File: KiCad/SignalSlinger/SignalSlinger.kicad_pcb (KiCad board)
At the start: 2 copper layers, 94.1 x 59.1 mm, 111 parts, among them J101 Conn_01x02, J102 Conn_01x03, J103 Conn_01x02, J104 Conn_01x02, J105 Conn_01x04, J106 Conn_01x02, J107 DB9 Female, J109 SolderJumper_2_Bridged, J201 Barrel_Jack_Switch, J203 External Fan Power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

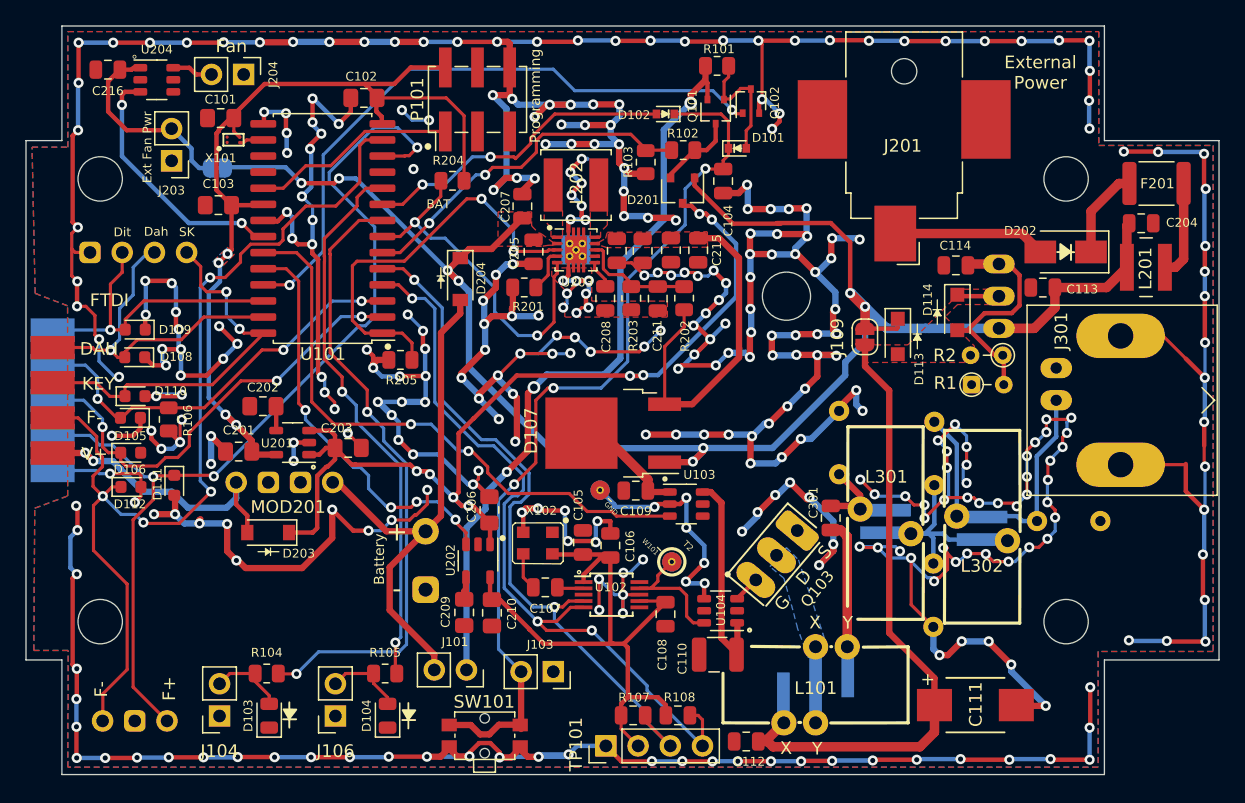
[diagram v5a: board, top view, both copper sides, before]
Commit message: Schematic & PCB Updates
o Improvements to DC power routing
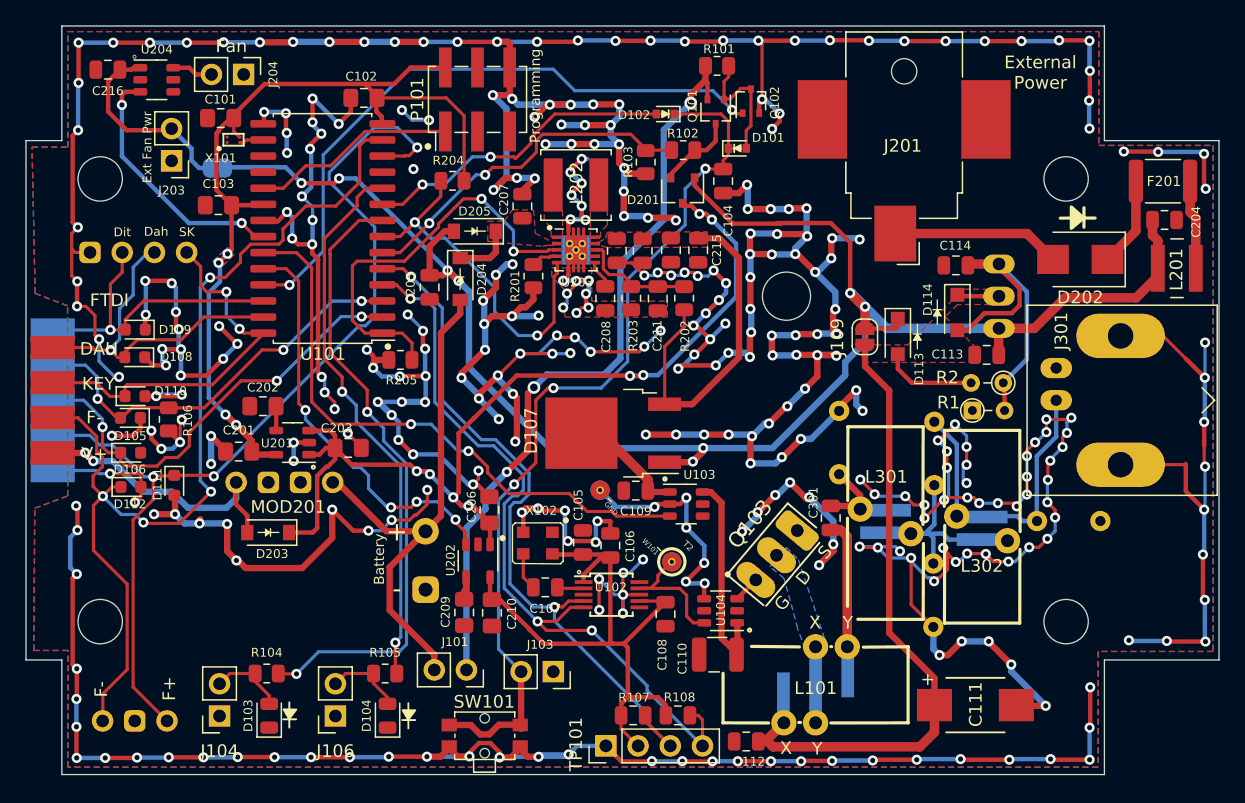
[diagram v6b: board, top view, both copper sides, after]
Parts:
- added D205: Schottky Diode, Diode_SMD:D_SOD-123, F.Cu at (81.4, 76.1)
- D202: footprint Diode_SMD:D_SMA -> Diode_SMD:D_SMB
- moved C205 8.66 mm to (77.8, 80.5)
- moved C113 6.92 mm to (121.8, 85.8)
- moved L201 2.44 mm to (136.8, 79.0)
- moved R2 2.18 mm to (123.1, 88.0)
- moved R1 2.04 mm to (120.7, 90.2)
- moved C204 1.86 mm to (135.8, 75.2)
- moved D202 1.29 mm to (129.2, 78.3)
- moved R201 1.14 mm to (86.0, 79.6), turned to -90 degrees
- moved F201 0.54 mm to (135.7, 72.1)
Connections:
- C207 pad 2: V_ext -> Net-(C207-Pad2)
- D204 pad 1: V_ext -> Net-(C207-Pad2)
- U203 pad 2: V_ext -> Net-(C207-Pad2)
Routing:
- net GND: track 883.3 -> 870.5 mm, vias 352 -> 349
- net Net-(C111-Pad1): track 52.7 -> 59.9 mm
- net Net-(C114-Pad1): track 18.3 -> 24.8 mm
- net Net-(C207-Pad2): track 0.00 -> 4.64 mm
- net V_ext: track 140.1 -> 142.4 mm
- net Net-(R201-Pad1): track 3.20 -> 1.87 mm
- net Net-(D202-Pad2): track 12.0 -> 13.3 mm
- net Net-(F201-Pad1): track 7.71 -> 7.06 mm
- added copper zone on F.Cu, net Net-(C207-Pad2)
- removed copper zone on F.Cu, net V_ext
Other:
- board text added: "SignalSlinger github.com/OpenARDF/SignalSlinger Open Source: MIT License Model: SS-80 Dec 2023"
- board text removed: "BAT"
- board text removed: "SignalSlinger github.com/OpenARDF/SignalSlinger Open Source: MIT License Model: SS-80 Nov 2023"

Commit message: Schematic Update
o Power routing improvement
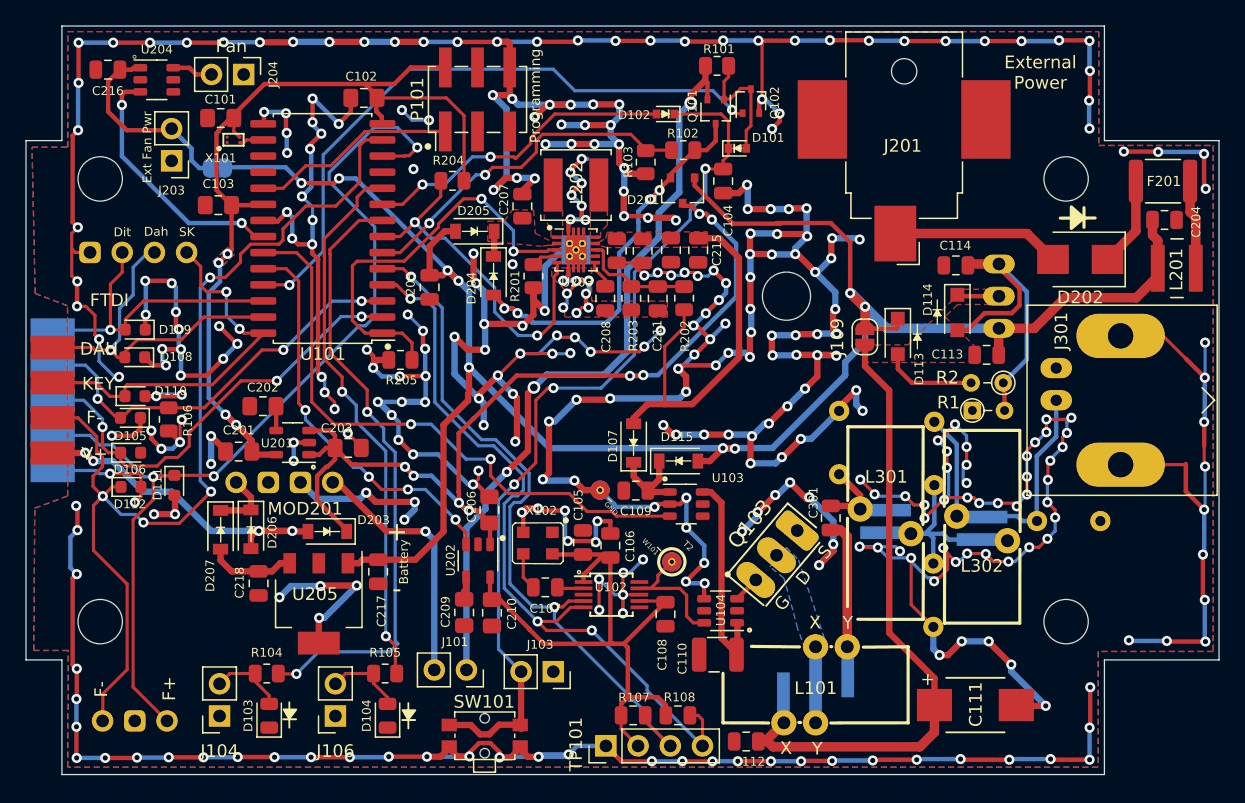
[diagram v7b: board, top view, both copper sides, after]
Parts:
- removed BT201: LiIon Cell, Connector_Wire:SolderWire-0.5sqmm_1x02_P4.6mm_D0.9mm_OD2.1mm
- added C217: 330nF, Capacitor_SMD:C_0805_2012Metric, F.Cu at (73.8, 102.9)
- added C218: 100nF, Capacitor_SMD:C_0805_2012Metric, F.Cu at (64.3, 103.9)
- added D115: Schottky Diode, Diode_SMD:D_SOD-123FL, F.Cu at (97.5, 94.2)
- added D206: Schottky Diode, Diode_SMD:D_SOD-123FL, F.Cu at (63.8, 99.6)
- added D207: Schottky Diode, Diode_SMD:D_SOD-123FL, F.Cu at (61.4, 99.6)
- added U205: uA7805, Package_TO_SOT_SMD:SOT-223-4, F.Cu at (69.1, 105.4)
- D107: value MBRD10100CT -> Schottky Diode; footprint Package_TO_SOT_SMD:TO-252-2 -> Diode_SMD:D_SOD-123FL
- D203, D204, D205: footprint Diode_SMD:D_SOD-123 -> Diode_SMD:D_SOD-123FL
- moved D203 4.66 mm to (69.8, 99.8)
- moved D204 2.63 mm to (82.9, 79.6)
- moved D107 1.92 mm to (93.9, 92.8), turned to 90 degrees
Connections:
- D107 pad 1: V_ext -> Net-(C109-Pad2)
- D107 pad 2: Net-(C109-Pad2) -> +7V
- D204 pad 2: +BATT -> +VSW
- MOD201 pad 4: V+_Charging -> Net-(D206-Pad1)
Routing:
- net GND: track 870.5 -> 898.7 mm, vias 349 -> 355
- net +VSW: track 5.97 -> 31.7 mm, vias 0 -> 4
- net +BATT: track 41.5 -> 19.8 mm, vias 0 -> 1
- net V_ext: track 142.4 -> 164.0 mm, vias 8 -> 9
- net Net-(C218-Pad1): track 0.00 -> 6.84 mm
- net Net-(D206-Pad1): track 0.00 -> 5.00 mm
- net V+_Charging: track 23.1 -> 28.1 mm, vias 2 -> 4
- net +7V: track 27.2 -> 30.6 mm
- net Net-(C207-Pad2): track 4.64 -> 1.89 mm
- net Net-(C203-Pad2): track 77.2 -> 75.8 mm
- net Net-(R104-Pad2): track 49.7 -> 48.8 mm
- net V3V3_PWR_ENABLE: track 32.7 -> 31.8 mm
- net Net-(C109-Pad2): track 7.83 -> 7.18 mm
- net FET_DRIVER_ENABLE: track 47.3 -> 47.8 mm
